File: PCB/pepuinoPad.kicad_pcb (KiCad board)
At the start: 2 copper layers, 203 x 176 mm, 246 parts, among them U1 Raspberry_Pi_Pico

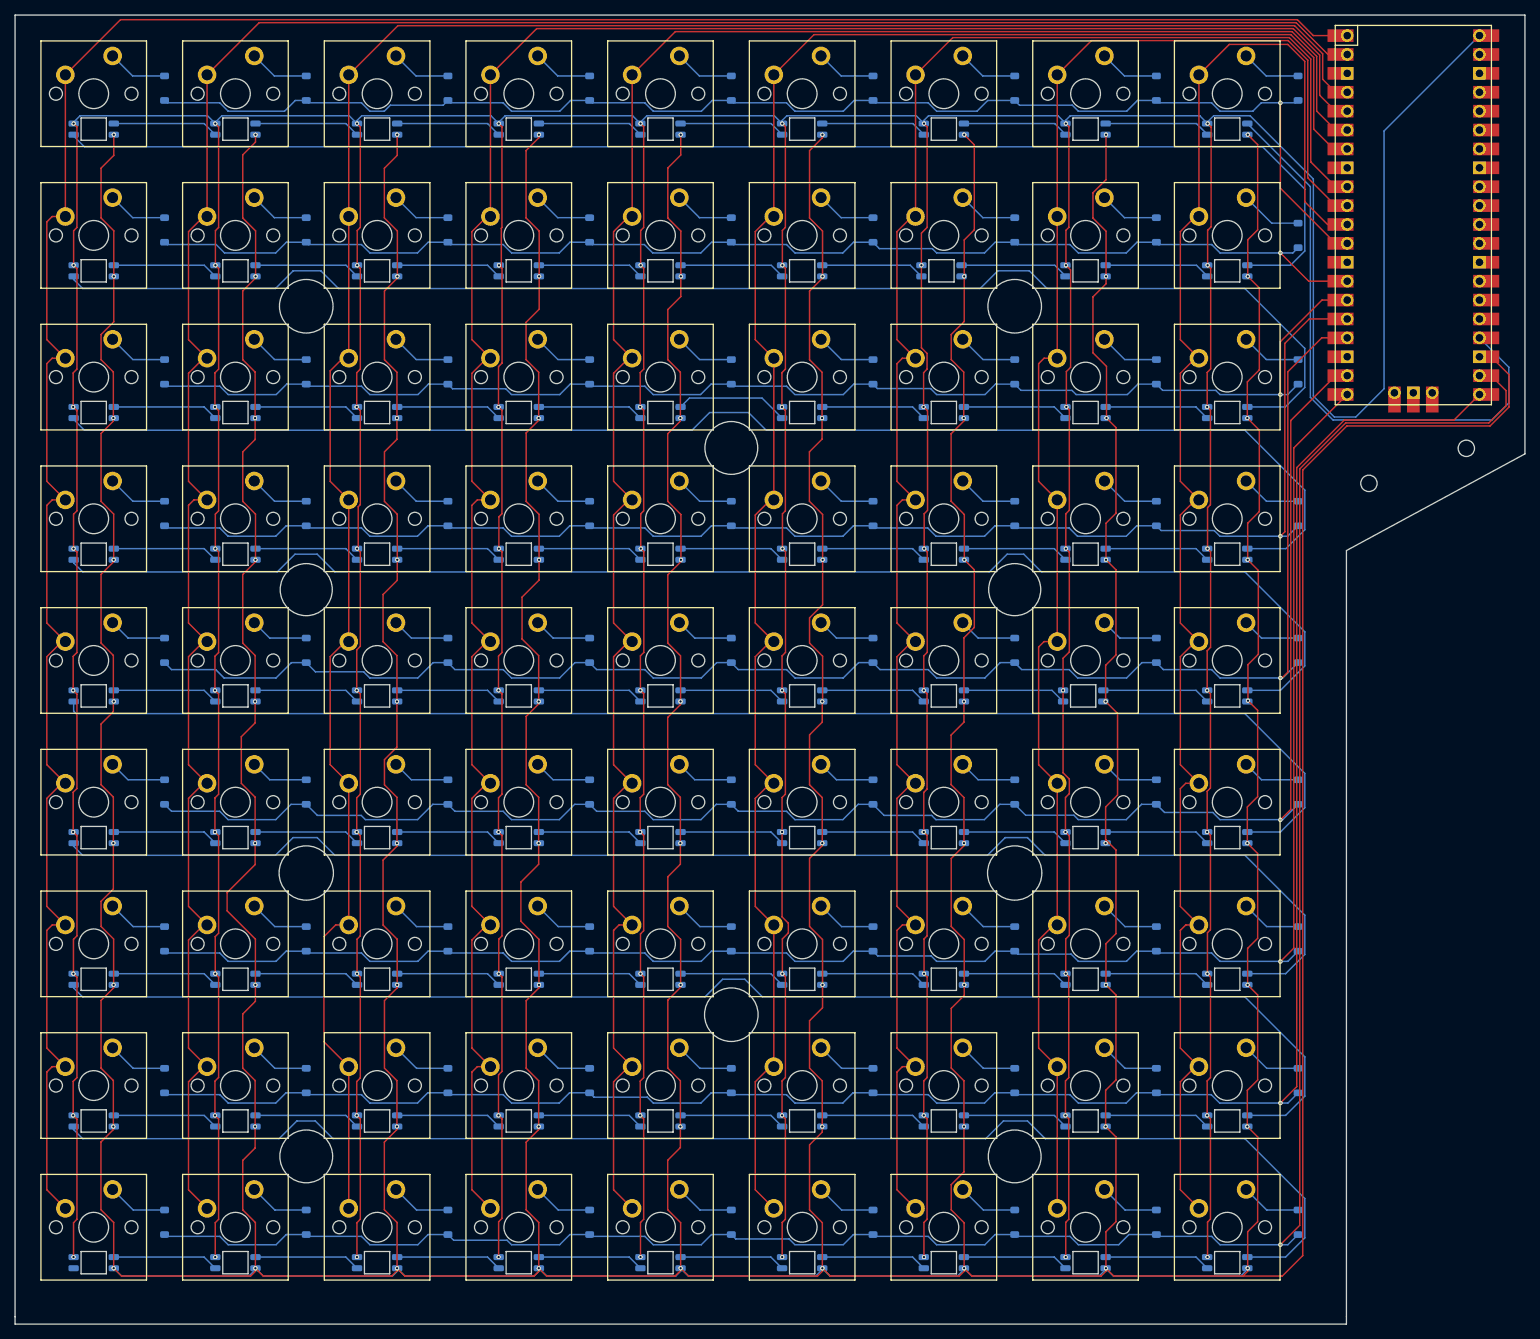
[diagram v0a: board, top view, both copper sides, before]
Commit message: add roatry encododer + pepuino nano + update readme and img
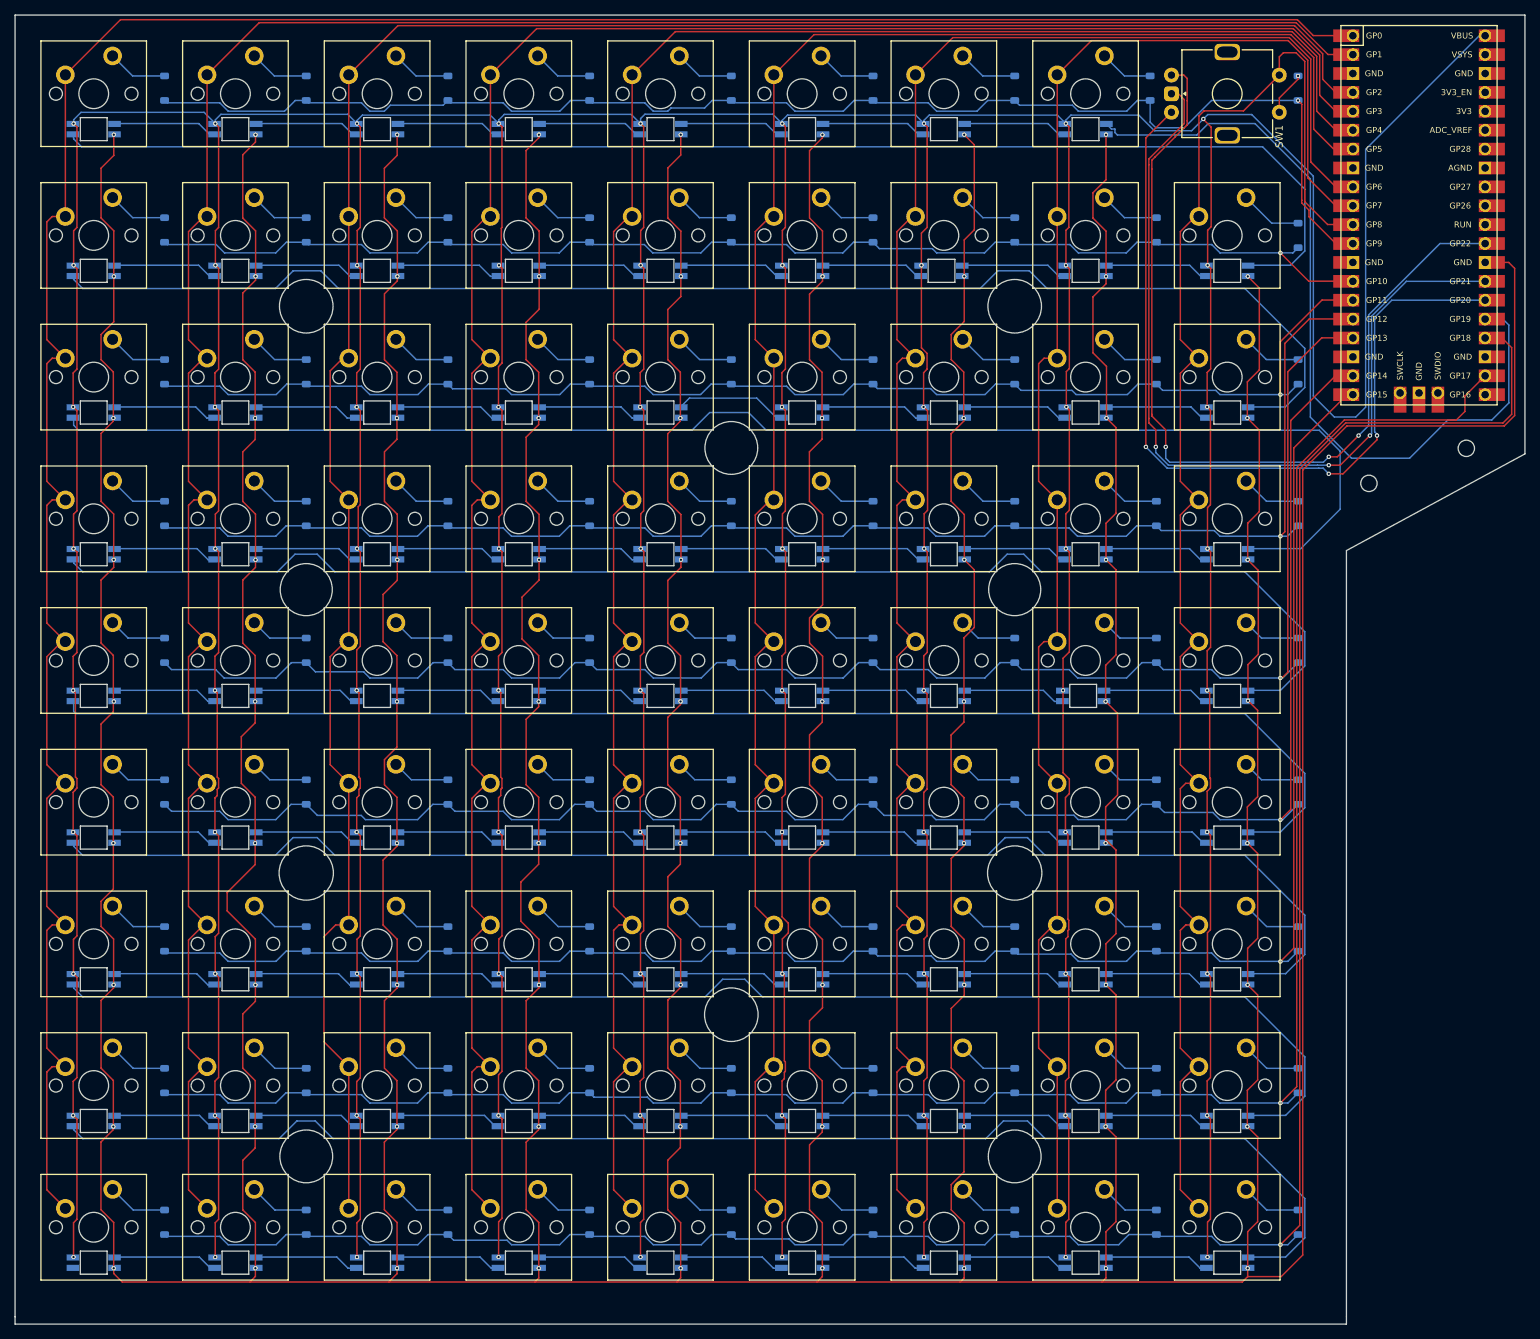
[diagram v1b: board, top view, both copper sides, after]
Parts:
- removed D82: LED_SK6812MINI, ScottoKeebs_Components:LED_SK6812MINI
- removed S9: ~, ScottoKeebs_MX:MX_PCB_1.00u
- added SW1: RotaryEncoder_Switch, PCM_marbastlib-various:ROT_Alps_EC11E-Switch, F.Cu at (181.0, 28.6)
- D100, D101, D102, D103, D104, D105, D106, D107, D108, D109, D110, D111, D112, D113, D114, D115, D116, D117, D118, D119, D120, D121, D122, D123, D124, D125, D126, D127, D128, D129, D130, D131, D132, D133, D134, D135, D136, D137, D138, D139, D140, D141, D142, D143, D144, D145, D146, D147, D148, D149, D150, D151, D152, D153, D154, D155, D156, D157, D158, D159, D160, D161, D162, D83, D84, D85, D86, D87, D88, D89, D90, D91, D92, D93, D94, D95, D96, D97, D98, D99: footprint ScottoKeebs_Components:LED_SK6812MINI -> kbd:YS-SK6812MINI-E
- moved D8 0.84 mm to (170.6, 27.8)
- moved U1 0.76 mm to (206.8, 44.9)
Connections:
- D83 pad 4: Net-(D82-DOUT) -> LED
- U1 pad 21: ROW7 -> unconnected-(U1-GPIO16-Pad21)
- U1 pad 22: ROW8 -> ROW7
- U1 pad 23: GND -> unconnected-(U1-GND-Pad23)
- U1 pad 24: LED -> ROW8
- U1 pad 25: unconnected-(U1-GPIO19-Pad25) -> LED
- U1 pad 26: unconnected-(U1-GPIO20-Pad26)_1 -> encoderB
- U1 pad 27: unconnected-(U1-GPIO21-Pad27)_1 -> encoderC
- U1 pad 28: unconnected-(U1-GND-Pad28)_1 -> GND
- U1 pad 29: unconnected-(U1-GPIO22-Pad29)_1 -> encoderA
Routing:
- net GND: track 1948.5 -> 1793.2 mm, vias 81 -> 80
- net encoderA: track 0.00 -> 120.2 mm, vias 0 -> 3
- net encoderC: track 0.00 -> 116.5 mm, vias 0 -> 3
- net encoderB: track 0.00 -> 113.3 mm, vias 0 -> 3
- net LED: track 79.6 -> 110.2 mm
- net Net-(D82-DOUT): track 14.3 -> 0.00 mm
- net Net-(D108-DOUT): track 185.6 -> 197.0 mm
- net ROW8: track 300.9 -> 307.1 mm
- net VBUS: track 1672.1 -> 1676.0 mm
- net ROW0: track 180.3 -> 184.1 mm
- net ROW7: track 274.0 -> 277.1 mm
- net COL8: track 210.7 -> 208.0 mm
- net Net-(D9-A): track 8.10 -> 5.94 mm, vias 0 -> 1
- net Net-(D91-DOUT): track 14.3 -> 13.4 mm
- net Net-(D83-DOUT): track 14.3 -> 13.4 mm
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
